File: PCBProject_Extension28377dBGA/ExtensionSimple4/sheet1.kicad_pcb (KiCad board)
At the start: 4 copper layers, 153.2 x 142.2 mm, 353 parts, among them J1 Conn_02x05_Odd_Even, J2 Conn_02x05_Odd_Even, J3 Conn_02x05_Odd_Even, J4 Conn_02x05_Odd_Even, Q1 FMMT618TA, U1 SN74ABT541, U2 SN74ABT541, U3 SN74ABT541, U4 SN74ABT541, U5 ADR423ARZ

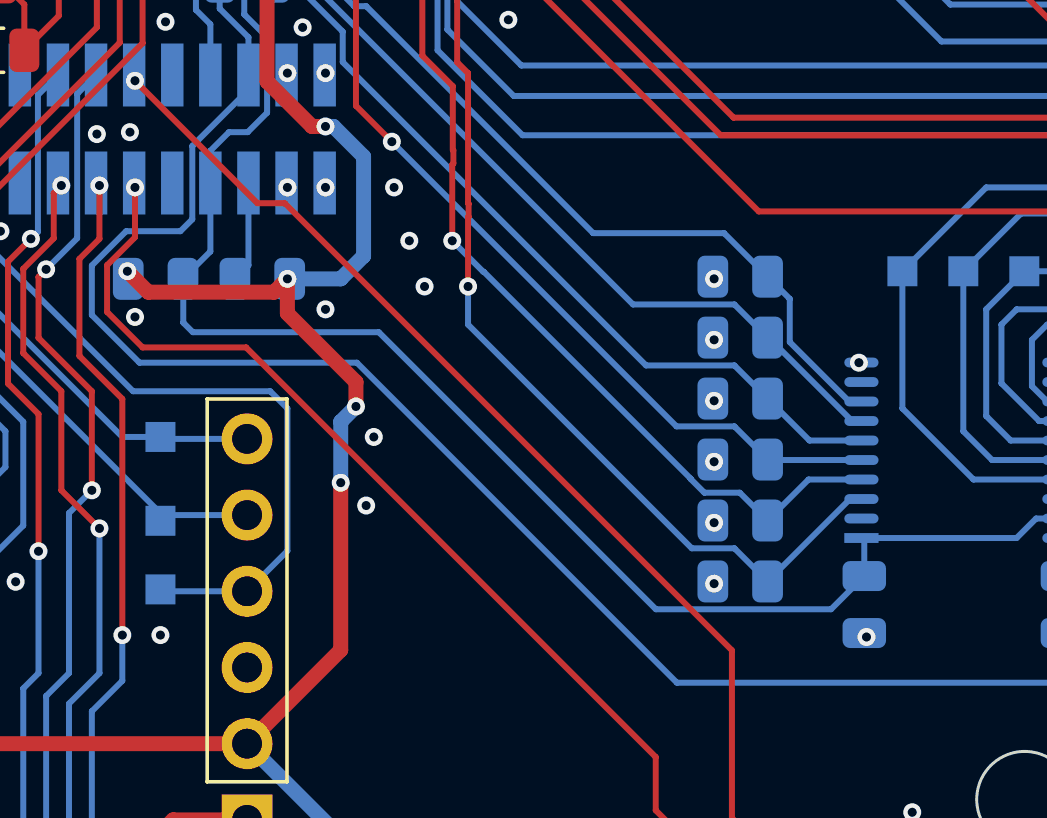
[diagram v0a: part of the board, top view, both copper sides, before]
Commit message: 重定义了DAC接口和修复了底板的PWM的bug，还需实现DAC电源集成
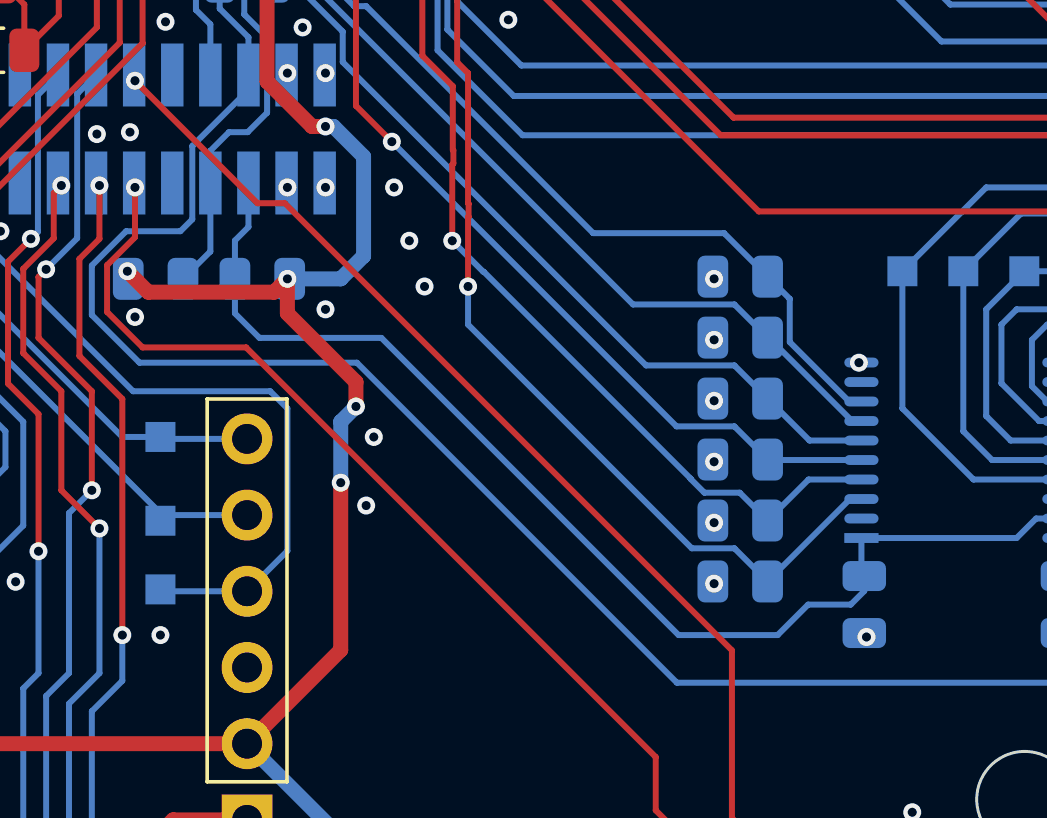
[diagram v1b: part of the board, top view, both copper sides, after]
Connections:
- C2 pad 2: /DSP_PWM3~{_ENABL}E -> /DSP_PWM4~{_ENABL}E
- U2 pad 1: /DSP_PWM3~{_ENABL}E -> /DSP_PWM4~{_ENABL}E
- U2 pad 19: /DSP_PWM3~{_ENABL}E -> /DSP_PWM4~{_ENABL}E
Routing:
- net /DSP_PWM3~{_ENABL}E: track 118.8 -> 82.1 mm
- net /DSP_PWM4~{_ENABL}E: track 3.38 -> 39.2 mm
